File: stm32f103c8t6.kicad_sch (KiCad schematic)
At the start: 0 parts

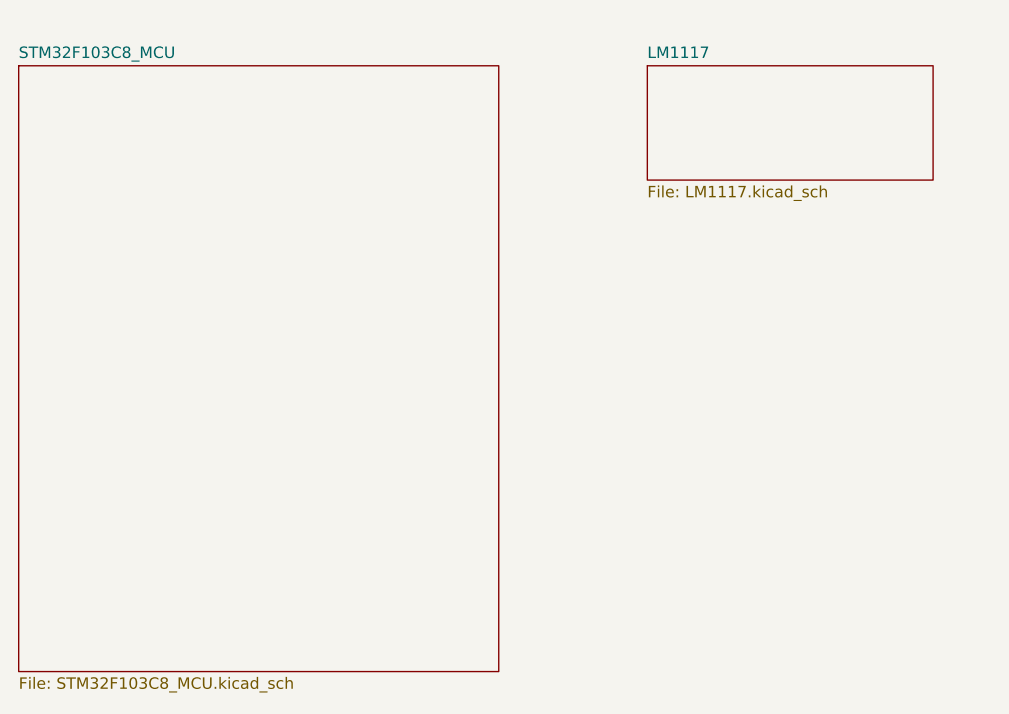
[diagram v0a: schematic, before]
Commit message: Update schematics and add LED circuit
- Add led.kicad_sch (new LED subcircuit)
- Update STM32F103C8_MCU schematic
- Update top-level schematic and project file
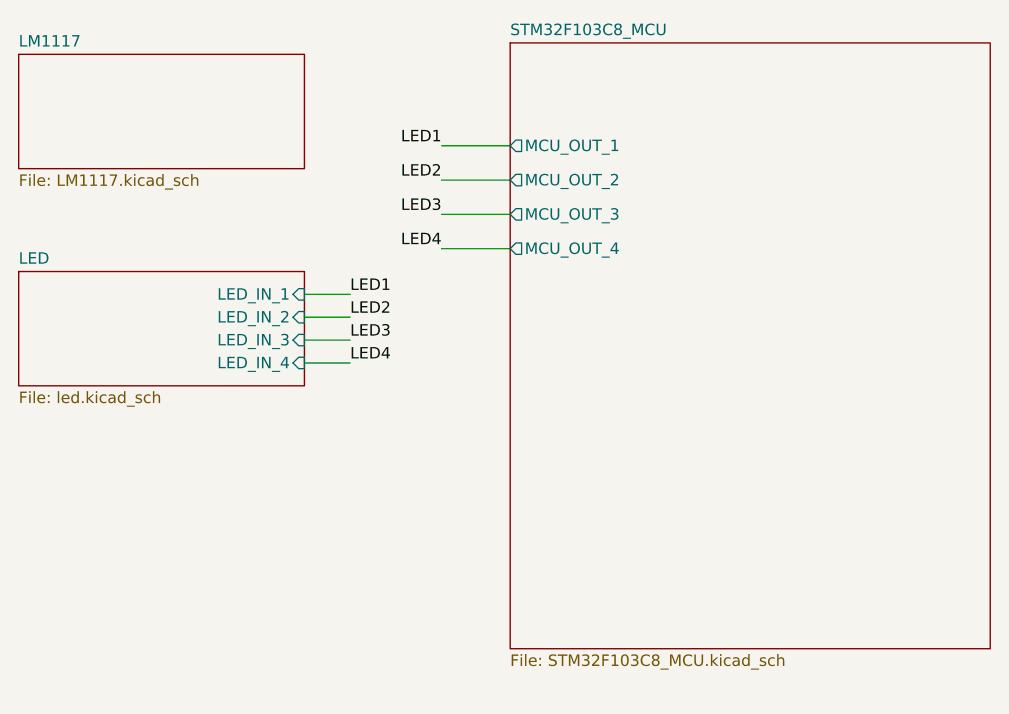
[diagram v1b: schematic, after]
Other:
- added sheet LED (led.kicad_sch)
- sheet STM32F103C8_MCU ports: added MCU_OUT_1, MCU_OUT_2, MCU_OUT_3, MCU_OUT_4; removed none
